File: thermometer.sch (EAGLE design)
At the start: 39 parts, among them IC1 MAX232, J1 MICRO-USB-5P-340015001, Q2 4 MHz, T1 BC547, T2 BC547, T3 BC547, T6 BC547, T7 BC547, T8 BC547, T9 BC547

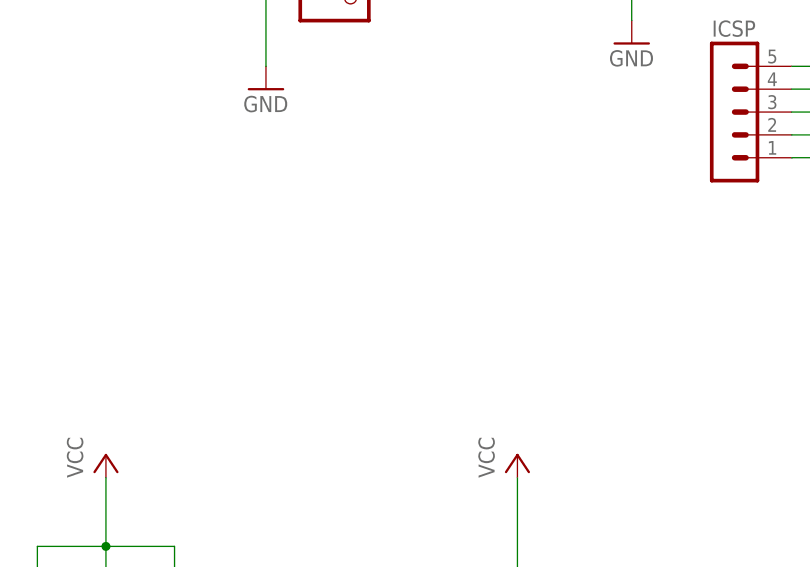
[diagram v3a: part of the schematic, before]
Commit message: Adding some text and Open Hardware logo
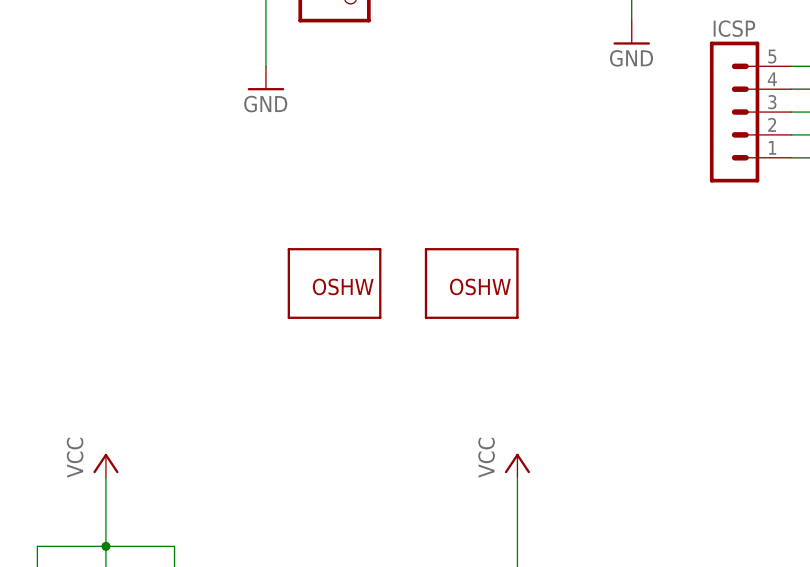
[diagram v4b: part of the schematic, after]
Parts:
- added GOLD_ORB_SM1: OSHWLOGO_GOLD_ORB_LG, NBitWonder:OSHWLOGO_GOLD_ORB_LG
- added GOLD_ORB_SM2: OSHWLOGO_GOLD_ORB_SM, NBitWonder:OSHWLOGO_GOLD_ORB_SM
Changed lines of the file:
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@@
 <part name="J1" library="Connector" deviceset="MICRO-USB-5P" device="-340015001"/>
 <part name="GND21" library="supply1" deviceset="GND" device=""/>
+<part name="GOLD_ORB_SM1" library="NBitWonder" deviceset="OSHWLOGO" device="_GOLD_ORB_LG"/>
+<part name="GOLD_ORB_SM2" library="NBitWonder" deviceset="OSHWLOGO" device="_GOLD_ORB_SM"/>
 </parts>
 <sheets>
@@
 <instance part="J1" gate="USB" x="-78.74" y="231.14"/>
 <instance part="GND21" gate="1" x="-66.04" y="218.44"/>
+<instance part="GOLD_ORB_SM1" gate="G$1" x="-88.9" y="187.96"/>
+<instance part="GOLD_ORB_SM2" gate="G$1" x="-104.14" y="187.96"/>
 </instances>
 <busses>
